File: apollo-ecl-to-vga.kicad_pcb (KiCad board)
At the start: 2 copper layers, 64 x 36.2 mm, 11 parts, among them IC1 SY100ELT25ZG-TR, J1 DB9_Female, J2 DB15_Female

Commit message: label nets from usb connector
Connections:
- net Net-(PS1-+Vin) renamed /USB_Vbus
- net Net-(PS1--Vin) renamed /USB_GND

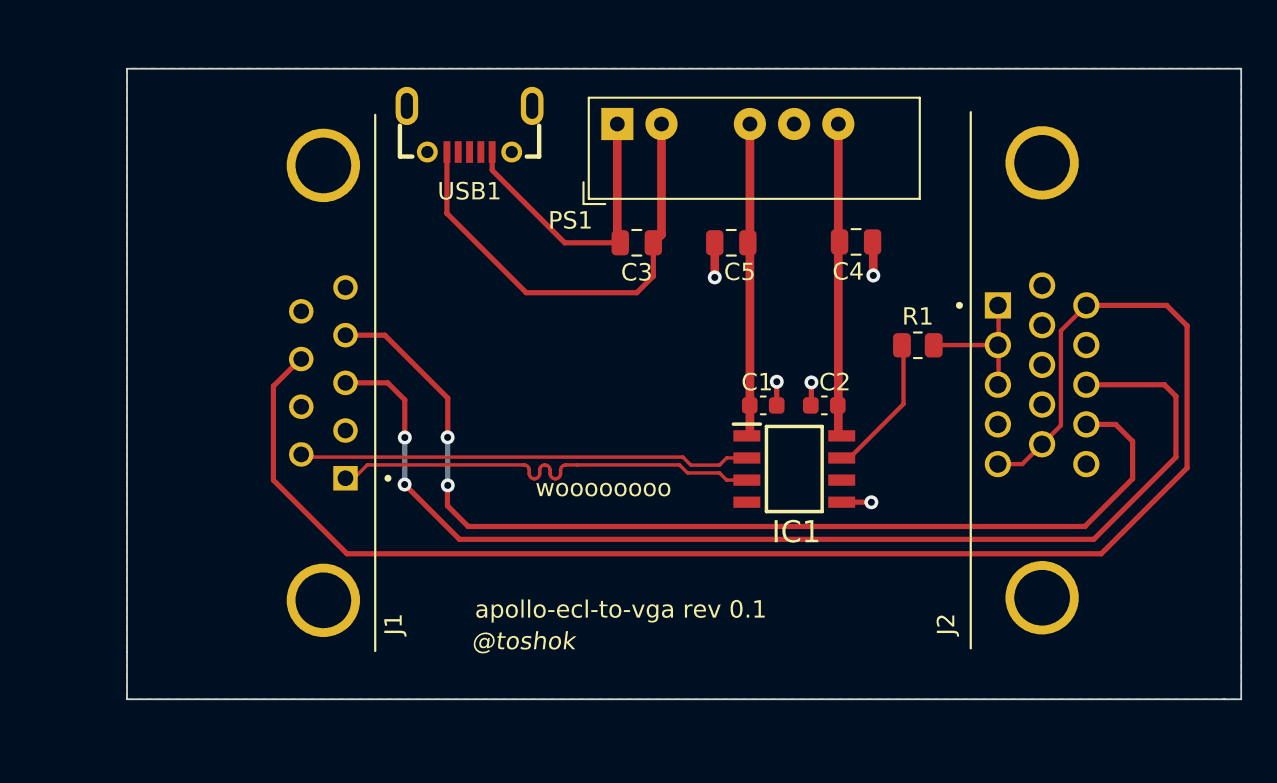
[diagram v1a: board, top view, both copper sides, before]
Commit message: add more resistors
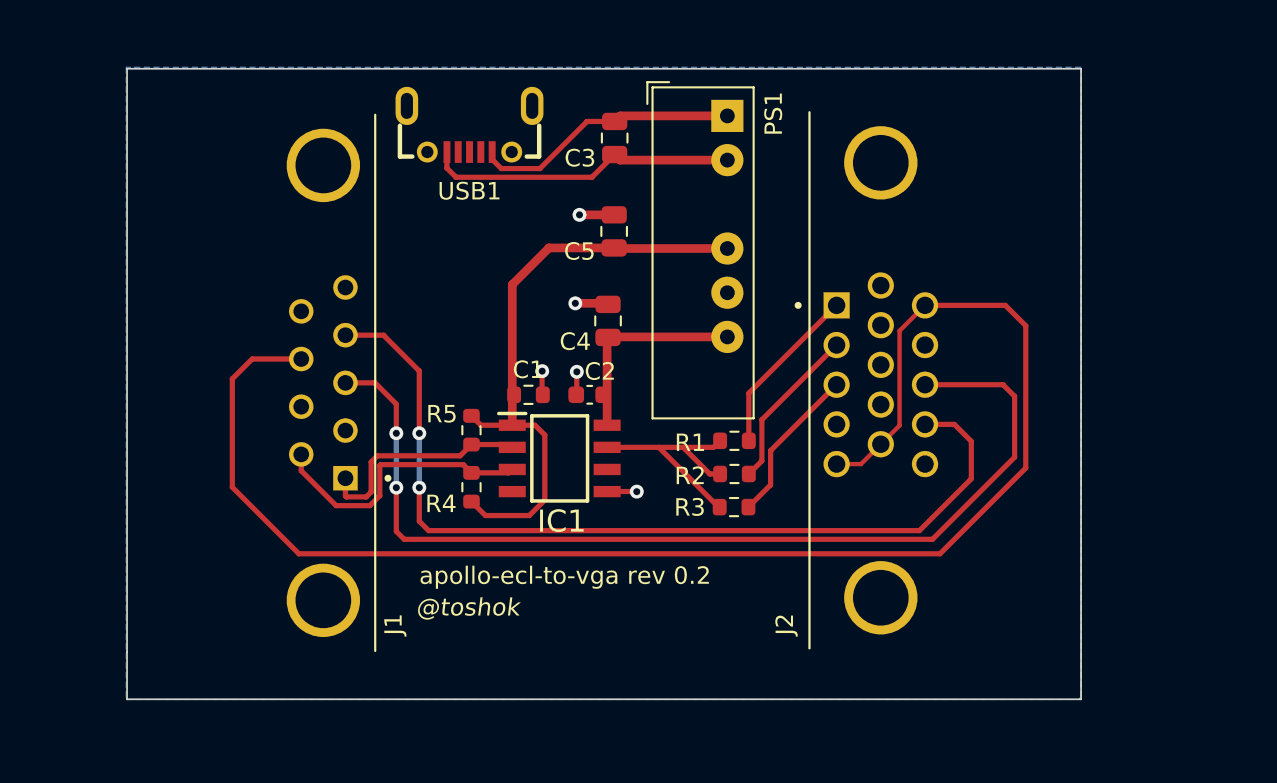
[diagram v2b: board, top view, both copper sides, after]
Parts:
- added R2: 390, Resistor_SMD:R_0603_1608Metric, F.Cu at (100.9, 94.2)
- added R3: 390, Resistor_SMD:R_0603_1608Metric, F.Cu at (100.8, 96.1)
- added R4: 470, Resistor_SMD:R_0603_1608Metric, F.Cu at (85.8, 95.0)
- added R5: 470, Resistor_SMD:R_0603_1608Metric, F.Cu at (85.8, 91.7)
- C1: footprint Capacitor_SMD:C_0603_1608Metric -> Resistor_SMD:R_0603_1608Metric
- R1: value 150 -> 390; footprint Resistor_SMD:R_0805_2012Metric -> Resistor_SMD:R_0603_1608Metric
- moved C4 15.0 mm to (93.6, 85.4), turned to 90 degrees
- moved C1 13.5 mm to (89.0, 89.7)
- moved C2 13.5 mm to (92.5, 89.7)
- moved IC1 13.5 mm to (90.8, 93.3)
- moved R1 11.9 mm to (100.9, 92.3), turned to 180 degrees
- moved J2 9.27 mm to (109.3, 88.9)
- moved C5 6.76 mm to (93.9, 80.3), turned to -90 degrees
- moved PS1 6.34 mm to (100.5, 73.7), turned to 0 degrees
- moved C3 6.15 mm to (94.0, 74.9), turned to -90 degrees
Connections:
- IC1 pad 7: Net-(IC1-Q) -> /video_out
- J1 pad 01: /video- -> /video+
- J1 pad 06: /video+ -> /video-
- J2 pad 1: Net-(J2-Pad1) -> /red
- J2 pad 2: Net-(J2-Pad1) -> /green
- J2 pad 3: Net-(J2-Pad1) -> /blue
- R1 pad 1: Net-(IC1-Q) -> /red
- R1 pad 2: Net-(J2-Pad1) -> /video_out
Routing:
- net -5V: track 18.0 -> 34.7 mm
- net /video_out: track 0.00 -> 14.3 mm
- net /video+: track 25.6 -> 13.0 mm
- net /red: track 0.00 -> 9.87 mm
- net /green: track 0.00 -> 9.50 mm
- net /video-: track 25.5 -> 16.2 mm
- net /blue: track 0.00 -> 9.13 mm
- net /USB_GND: track 26.6 -> 17.9 mm
- net Net-(J2-Pad1): track 8.36 -> 0.00 mm
- net Net-(IC1-Q): track 8.21 -> 0.00 mm
- net /hsync: track 65.1 -> 57.3 mm
- net /vsync: track 59.8 -> 52.1 mm
- net +5V: track 18.0 -> 11.9 mm
- net /sync_gnd: track 90.4 -> 86.3 mm
- net /USB_Vbus: track 17.0 -> 15.4 mm
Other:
- board size 64 x 36.2 mm -> 54.8 x 36.2 mm
- board text added: "apollo-ecl-to-vga rev 0.2"
- board text removed: "apollo-ecl-to-vga rev 0.1"
- board text removed: "woooooooo"

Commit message: route sync_gnd on the back
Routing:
- net /sync_gnd: track 86.3 -> 77.7 mm, vias 0 -> 1
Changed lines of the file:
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@@
   (via (at 82.7532 95.0214) (size 0.8) (drill 0.4) (layers "F.Cu" "B.Cu") (net 9))
   (segment (start 82.7532 91.8972) (end 82.7532 95.0214) (width 0.3) (layer "B.Cu") (net 9))
-  (segment (start 117.602 85.72) (end 117.602 93.89) (width 0.3) (layer "F.Cu") (net 10))
-  (segment (start 109.272 92.52675) (end 108.132 93.66675) (width 0.25) (layer "F.Cu") (net 10))
-  (segment (start 116.42875 84.54675) (end 117.602 85.72) (width 0.3) (layer "F.Cu") (net 10))
-  (segment (start 110.351 86.00775) (end 110.351 91.44775) (width 0.25) (layer "F.Cu") (net 10))
-  (segment (start 112.672 98.82) (end 75.833 98.82) (width 0.3) (layer "F.Cu") (net 10))
-  (segment (start 72.009 88.773) (end 73.152 87.63) (width 0.3) (layer "F.Cu") (net 10))
-  (segment (start 117.602 93.89) (end 112.672 98.82) (width 0.3) (layer "F.Cu") (net 10))
-  (segment (start 72.009 94.996) (end 72.009 88.773) (width 0.3) (layer "F.Cu") (net 10))
-  (segment (start 75.833 98.82) (end 72.009 94.996) (width 0.3) (layer "F.Cu") (net 10))
-  (segment (start 111.812 84.54675) (end 110.351 86.00775) (width 0.25) (layer "F.Cu") (net 10))
-  (segment (start 108.132 93.66675) (end 106.732 93.66675) (width 0.25) (layer "F.Cu") (net 10))
-  (segment (start 73.152 87.63) (end 75.97 87.63) (width 0.3) (layer "F.Cu") (net 10))
-  (segment (start 111.8495 84.54675) (end 116.42875 84.54675) (width 0.3) (layer "F.Cu") (net 10))
-  (segment (start 110.351 91.44775) (end 109.272 92.52675) (width 0.25) (layer "F.Cu") (net 10))
+  (segment (start 75.97 87.63) (end 74.041 87.63) (width 0.3) (layer "F.Cu") (net 10))
+  (segment (start 73.0758 88.5952) (end 73.0758 89.9922) (width 0.3) (layer "F.Cu") (net 10))
+  (segment (start 74.041 87.63) (end 73.0758 88.5952) (width 0.3) (layer "F.Cu") (net 10))
+  (via (at 73.0758 89.9922) (size 0.8) (drill 0.4) (layers "F.Cu" "B.Cu") (net 10))
+  (segment (start 106.6038 97.9678) (end 106.732 97.8396) (width 0.3) (layer "B.Cu") (net 10))
+  (segment (start 109.3216 97.9678) (end 111.5568 97.9678) (width 0.3) (layer "B.Cu") (net 10))
+  (segment (start 111.5568 97.9678) (end 115.5192 94.0054) (width 0.3) (layer "B.Cu") (net 10))
+  (segment (start 106.732 97.8396) (end 106.732 93.66675) (width 0.3) (layer "B.Cu") (net 10))
+  (segment (start 73.0758 95.5294) (end 75.5142 97.9678) (width 0.3) (layer "B.Cu") (net 10))
+  (segment (start 109.3216 97.9678) (end 109.272 97.9182) (width 0.3) (layer "B.Cu") (net 10))
+  (segment (start 106.6038 97.9678) (end 109.3216 97.9678) (width 0.3) (layer "B.Cu") (net 10))
+  (segment (start 115.5192 85.4964) (end 114.56955 84.54675) (width 0.3) (layer "B.Cu") (net 10))
+  (segment (start 114.56955 84.54675) (end 111.812 84.54675) (width 0.3) (layer "B.Cu") (net 10))
+  (segment (start 75.5142 97.9678) (end 106.6038 97.9678) (width 0.3) (layer "B.Cu") (net 10))
+  (segment (start 115.5192 94.0054) (end 115.5192 85.4964) (width 0.3) (layer "B.Cu") (net 10))
+  (segment (start 73.0758 89.9922) (end 73.0758 95.5294) (width 0.3) (layer "B.Cu") (net 10))
+  (segment (start 109.272 97.9182) (end 109.272 92.52675) (width 0.3) (layer "B.Cu") (net 10))
   (segment (start 92.673787 77.186213) (end 93.98 75.88) (width 0.3) (layer "F.Cu") (net 26))
   (segment (start 93.98 75.88) (end 94.3 76.2) (width 0.5) (layer "F.Cu") (net 26))

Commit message: more futzing
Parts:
- moved J2 1.28 mm to (110.5, 88.9)
- moved C1 1.04 mm to (90.1, 89.7)
- moved C4 1.04 mm to (94.6, 85.4)
- moved IC1 1.04 mm to (91.9, 93.3)
- moved J1 1.04 mm to (67.0, 89.0)
- moved PS1 1.04 mm to (101.5, 73.7)
- moved R4 1.04 mm to (86.8, 95.0)
- moved R5 1.04 mm to (86.8, 91.7)
- moved USB1 1.04 mm to (86.7, 74.4)
- moved C2 1.04 mm to (93.6, 89.7)
- moved C3 1.04 mm to (95.0, 74.9)
- moved C5 1.04 mm to (95.0, 80.3)
- moved R3 0.53 mm to (101.2, 96.5)
- moved R1 0.53 mm to (101.3, 92.7)
- moved R2 0.53 mm to (101.3, 94.6)
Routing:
- net /vsync: track 52.1 -> 65.9 mm, vias 2 -> 0
- net /hsync: track 57.3 -> 71.1 mm, vias 2 -> 0
- net /blue: track 9.13 -> 11.7 mm
- net /green: track 9.50 -> 11.7 mm
- net /video-: track 16.2 -> 14.4 mm
- net /red: track 9.87 -> 11.5 mm
- net /video+: track 13.0 -> 11.4 mm
- net /video_out: track 14.3 -> 15.8 mm
- net /sync_gnd: track 77.7 -> 78.3 mm, vias 1 -> 0
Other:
- board size 54.8 x 36.2 mm -> 55 x 36.2 mm
- board text added: "New hotness"
- board text added: "Old and busted"
- board text added: "apollo-ecl-to-vga rev 2"
- board text removed: "apollo-ecl-to-vga rev 0.2"

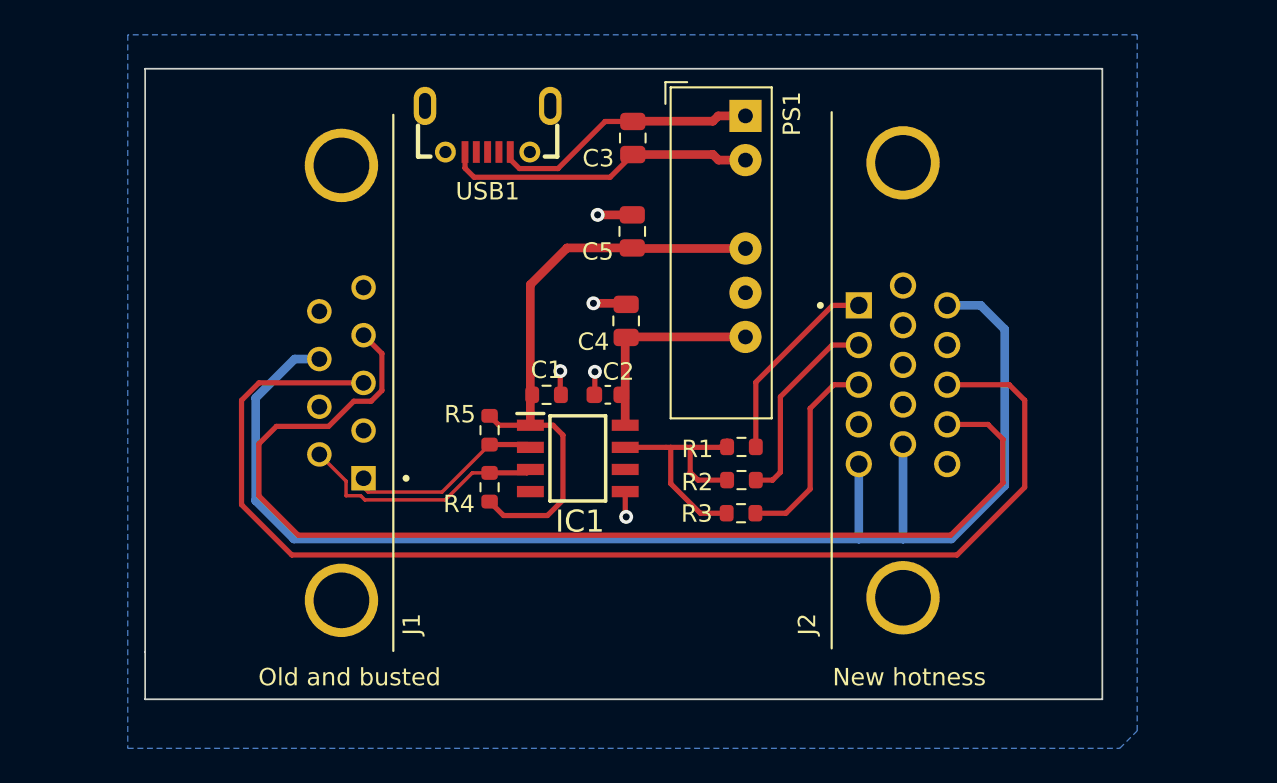
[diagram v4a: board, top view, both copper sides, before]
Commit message: single GND.  move things (vias, resistors, DC/DC) a touch to clean up routing, and cleanup some trace widths
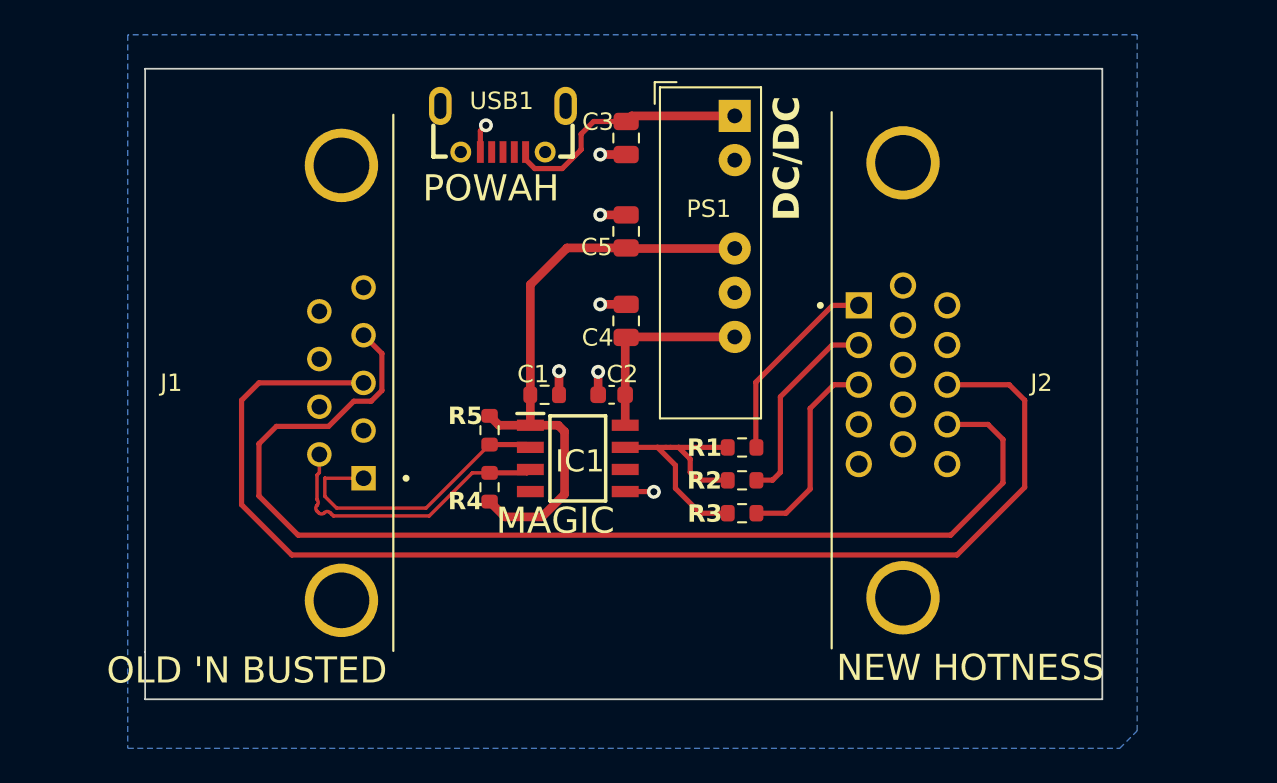
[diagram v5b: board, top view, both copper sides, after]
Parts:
- moved USB1 0.88 mm to (87.6, 74.4)
- moved PS1 0.62 mm to (100.9, 73.7)
- moved C3 0.38 mm to (94.6, 74.9)
- moved C5 0.35 mm to (94.6, 80.3)
- moved C2 0.22 mm to (93.8, 89.7)
- moved C1 0.11 mm to (90.0, 89.7)
- moved R3 0.06 mm to (101.3, 96.5)
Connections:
- C3 pad 2: /USB_GND -> GND
- J1 pad 08: /sync_gnd -> GND
- J2 pad 10: /sync_gnd -> GND
- J2 pad 11: /sync_gnd -> GND
- J2 pad 5: /sync_gnd -> GND
- PS1 pad 2: /USB_GND -> GND
- USB1 pad 5: /USB_GND -> GND
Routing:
- net /sync_gnd: track 78.3 -> 0.00 mm
- net /USB_GND: track 17.9 -> 0.00 mm
- net /video+: track 11.4 -> 16.9 mm
- net /video-: track 14.4 -> 16.9 mm
- net GND: track 8.17 -> 10.5 mm, vias 5 -> 7
- net /USB_Vbus: track 15.4 -> 14.0 mm
- net +5V: track 11.9 -> 11.3 mm
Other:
- board text added: "DC/DC"
- board text added: "NEW HOTNESS"
- board text added: "OLD 'N BUSTED"
- board text removed: "New hotness"
- board text removed: "Old and busted"
